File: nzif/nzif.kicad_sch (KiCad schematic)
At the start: 16 parts, among them J1 Rx, J10 ADAU1467_GPIOS, J11 ADAU1467_AUX_ADCS, J201 Rx, J4 6V, J6 Microcontroller, J7 USBi, J8 I2S2, J9 I2S1

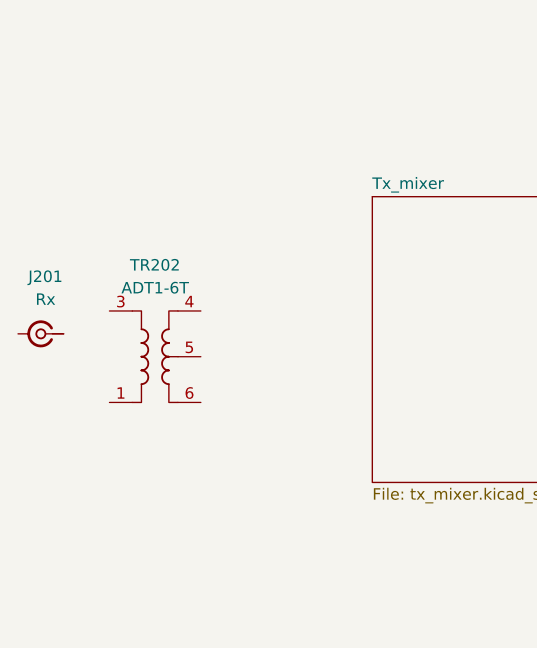
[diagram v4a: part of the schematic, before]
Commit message: added transformer for low band tx
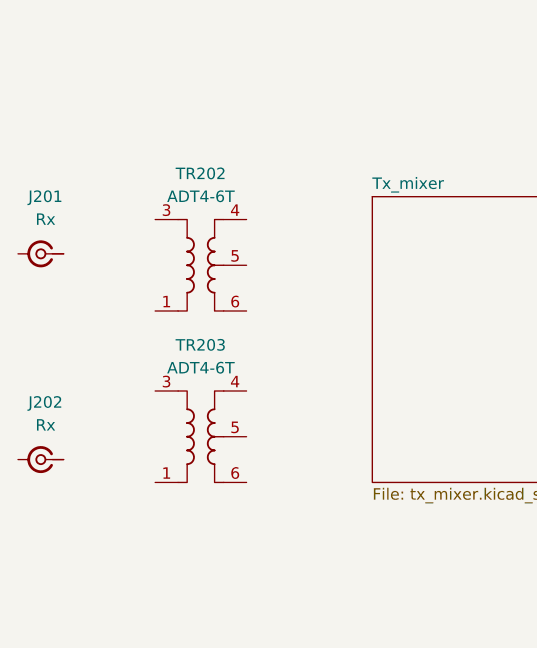
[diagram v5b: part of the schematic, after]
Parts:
- removed TR202: ADT1-6T, RF_Mini-Circuits:Mini-Circuits_CD637_H5.23mm, symbol Transformer:ADT1-6T
- added J202: Rx, symbol Connector:Conn_Coaxial_Small
- added TR202, TR203: ADT4-6T, RF_Mini-Circuits:Mini-Circuits_CD637_H5.23mm, symbol Transformer:ADT4-6T
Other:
- moved on the sheet: J201
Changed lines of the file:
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@@
+	)
+	(symbol
+		(lib_id "Transformer:ADT4-6T")
+		(at 46.99 144.78 0)
+		(unit 1)
+		(exclude_from_sim no)
+		(in_bom yes)
+		(on_board yes)
+		(dnp no)
+		(fields_autoplaced yes)
+		(property "Reference" "TR202"
+			(at 46.99 134.62 0)
+			(effects
+				(font
+					(size 1.27 1.27)
+				)
+			)
+		)
+		(property "Value" "ADT4-6T"
+			(at 46.99 137.16 0)
+			(effects
+				(font
+					(size 1.27 1.27)
+				)
+			)
+		)
+		(property "Footprint" "RF_Mini-Circuits:Mini-Circuits_CD637_H5.23mm"
+			(at 46.99 153.67 0)
+			(effects
+				(font
+					(size 1.27 1.27)
+				)
+				(hide yes)
+			)
+		)
+		(property "Datasheet" "https://www.minicircuits.com/pdfs/ADT4-6T+.pdf"
+			(at 46.99 144.78 0)
+			(effects
+				(font
+					(size 1.27 1.27)
+				)
+				(hide yes)
+			)
+		)
+		(property "Description" "1.5-70MHz 1:4 RF Transformer, Unbalanced to Balanced Center Tap, CD637"
+			(at 46.99 144.78 0)
+			(effects
+				(font
+					(size 1.27 1.27)
+				)
+				(hide yes)
+			)
+		)
+		(pin "3"
+		)
+		(pin "4"
+		)
+		(pin "6"
+		)
+		(pin "1"
+		)
+		(pin "5"
+		)
+		(instances
+			(project "nzif"
+				(path "/fe42ca2f-2bb8-4d5a-9e84-807788ed632f"
+					(reference "TR202")
+					(unit 1)
+				)
+			)
+		)
 	)
 	(symbol
@@
 	)
 	(symbol
-		(lib_id "Transformer:ADT1-6T")
-		(at 41.91 154.94 0)
-		(unit 1)
-		(exclude_from_sim no)
-		(in_bom yes)
-		(on_board yes)
-		(dnp no)
-		(fields_autoplaced yes)
-		(property "Reference" "TR202"
-			(at 41.91 144.78 0)
-			(effects
-				(font
-					(size 1.27 1.27)
-				)
-			)
-		)
-		(property "Value" "ADT1-6T"
-			(at 41.91 147.32 0)
-			(effects
-				(font
-					(size 1.27 1.27)
-				)
-			)
-		)
-		(property "Footprint" "RF_Mini-Circuits:Mini-Circuits_CD637_H5.23mm"
-			(at 41.91 163.83 0)
-			(effects
-				(font
-					(size 1.27 1.27)
-				)
-				(hide yes)
-			)
-		)
-		(property "Datasheet" "https://www.minicircuits.com/pdfs/ADT1-6T+.pdf"
-			(at 41.91 154.94 0)
-			(effects
-				(font
-					(size 1.27 1.27)
-				)
-				(hide yes)
-			)
-		)
-		(property "Description" "0.06-160MHz 1:1 RF Transformer, Unbalanced to Balanced Center Tap, CD542"
-			(at 41.91 154.94 0)
-			(effects
-				(font
-					(size 1.27 1.27)
-				)
-				(hide yes)
-			)
-		)
-		(pin "1"
-		)
-		(pin "5"
-		)
-		(pin "4"
-		)
-		(pin "6"
-		)
-		(pin "3"
-		)
-		(instances
-			(project "nzif"
-				(path "/fe42ca2f-2bb8-4d5a-9e84-807788ed632f"
-					(reference "TR202")
-					(unit 1)
-				)
-			)
-		)
-	)
-	(symbol
 		(lib_id "Device:R_Small_US")
 		(at 398.78 45.72 270)
@@
 	)
 	(symbol
+		(lib_id "Connector:Conn_Coaxial_Small")
+		(at 29.21 166.37 180)
+		(unit 1)
+		(exclude_from_sim no)
+		(in_bom yes)
+		(on_board yes)
+		(dnp no)
+		(fields_autoplaced yes)
+		(property "Reference" "J202"
+			(at 29.7295 160.02 0)
+			(effects
+				(font
+					(size 1.27 1.27)
+				)
+			)
+		)
+		(property "Value" "Rx"
+			(at 29.7295 162.56 0)
+			(effects
+				(font
+					(size 1.27 1.27)
+				)
+			)
+		)
+		(property "Footprint" ""
+			(at 29.21 166.37 0)
+			(effects
+				(font
+					(size 1.27 1.27)
+				)
+				(hide yes)
+			)
+		)
+		(property "Datasheet" "~"
+			(at 29.21 166.37 0)
+			(effects
+				(font
+					(size 1.27 1.27)
+				)
+				(hide yes)
+			)
+		)
+		(property "Description" "small coaxial connector (BNC, SMA, SMB, SMC, Cinch/RCA, LEMO, ...)"
+			(at 29.21 166.37 0)
+			(effects
+				(font
+					(size 1.27 1.27)
+				)
+				(hide yes)
+			)
+		)
+		(pin "2"
+		)
+		(pin "1"
+		)
+		(instances
+			(project "nzif"
+				(path "/fe42ca2f-2bb8-4d5a-9e84-807788ed632f"
+					(reference "J202")
+					(unit 1)
+				)
+			)
+		)
+	)
+	(symbol
 		(lib_id "Device:LED_Small_Filled")
 		(at 440.69 58.42 90)
@@
 	(symbol
 		(lib_id "Connector:Conn_Coaxial_Small")
-		(at 29.21 152.4 180)
+		(at 29.21 143.51 180)
 		(unit 1)
 		(exclude_from_sim no)
@@
 		(fields_autoplaced yes)
 		(property "Reference" "J201"
-			(at 29.7295 146.05 0)
+			(at 29.7295 137.16 0)
 			(effects
 				(font
@@
 		)
 		(property "Value" "Rx"
-			(at 29.7295 148.59 0)
-			(effects
-				(font
-					(size 1.27 1.27)
-				)
-			)
-		)
-		(property "Footprint" ""
-			(at 29.21 152.4 0)
+			(at 29.7295 139.7 0)
+			(effects
+				(font
+					(size 1.27 1.27)
+				)
+			)
+		)
+		(property "Footprint" ""
+			(at 29.21 143.51 0)
 			(effects
 				(font
@@
 		)
 		(property "Datasheet" "~"
-			(at 29.21 152.4 0)
+			(at 29.21 143.51 0)
 			(effects
 				(font
@@
 		)
 		(property "Description" "small coaxial connector (BNC, SMA, SMB, SMC, Cinch/RCA, LEMO, ...)"
-			(at 29.21 152.4 0)
+			(at 29.21 143.51 0)
 			(effects
 				(font
@@
 					(unit 1)
 				)
+			)
+		)
+	)
+	(symbol
+		(lib_id "Transformer:ADT4-6T")
+		(at 46.99 163.83 0)
+		(unit 1)
+		(exclude_from_sim no)
+		(in_bom yes)
+		(on_board yes)
+		(dnp no)
+		(fields_autoplaced yes)
+		(property "Reference" "TR203"
+			(at 46.99 153.67 0)
+			(effects
+				(font
+					(size 1.27 1.27)
+				)
+			)
+		)
+		(property "Value" "ADT4-6T"
+			(at 46.99 156.21 0)
+			(effects
+				(font
+					(size 1.27 1.27)
+				)
+			)
+		)
+		(property "Footprint" "RF_Mini-Circuits:Mini-Circuits_CD637_H5.23mm"
+			(at 46.99 172.72 0)
+			(effects
+				(font
+					(size 1.27 1.27)
+				)
+				(hide yes)
+			)
+		)
+		(property "Datasheet" "https://www.minicircuits.com/pdfs/ADT4-6T+.pdf"
+			(at 46.99 163.83 0)
+			(effects
+				(font
+					(size 1.27 1.27)
+				)
+				(hide yes)
+			)
+		)
+		(property "Description" "1.5-70MHz 1:4 RF Transformer, Unbalanced to Balanced Center Tap, CD637"
+			(at 46.99 163.83 0)
+			(effects
+				(font
+					(size 1.27 1.27)
+				)
+				(hide yes)
+			)
+		)
+		(pin "3"
+		)
+		(pin "4"
+		)
+		(pin "6"
+		)
+		(pin "1"
+		)
+		(pin "5"
+		)
+		(instances
+			(project "nzif"
+				(path "/fe42ca2f-2bb8-4d5a-9e84-807788ed632f"
+					(reference "TR203")
+					(unit 1)
+				)

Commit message: adjusted top level block positions
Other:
- moved on the sheet: D?, J10, J11, J8, J9, J?, R218, R219

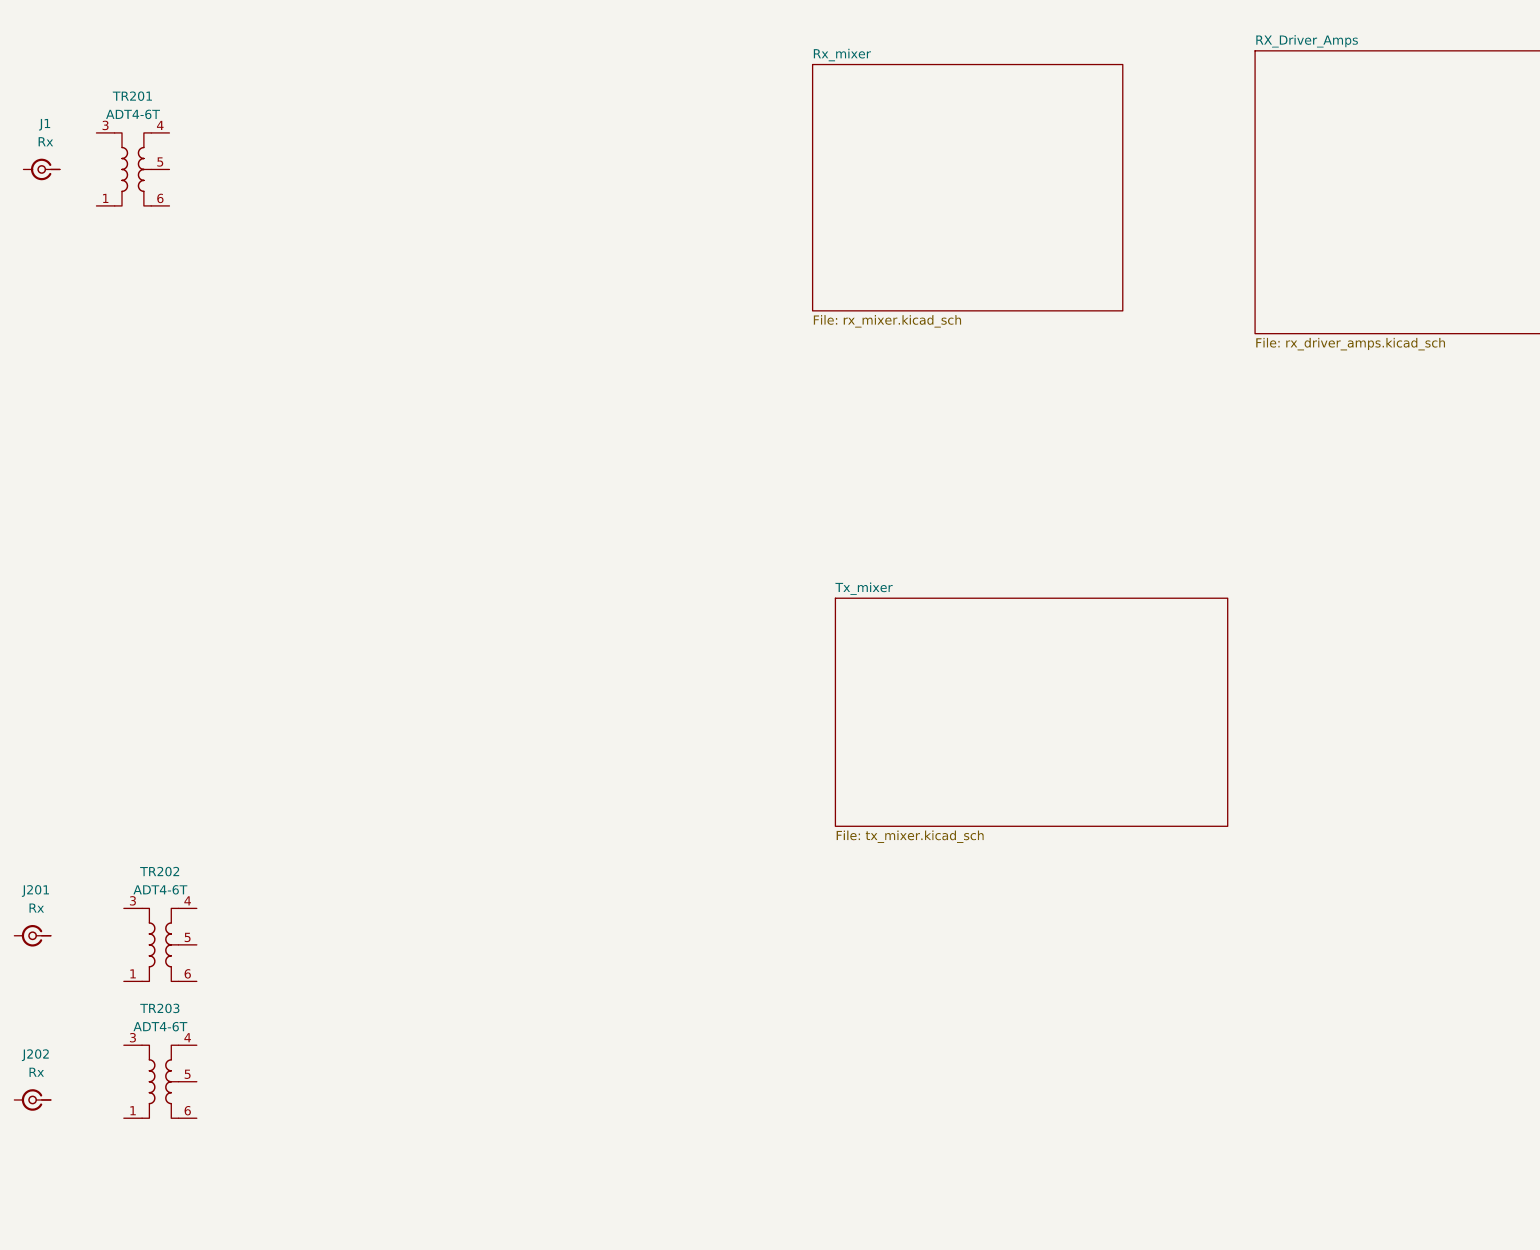
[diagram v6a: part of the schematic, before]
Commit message: added ad9912
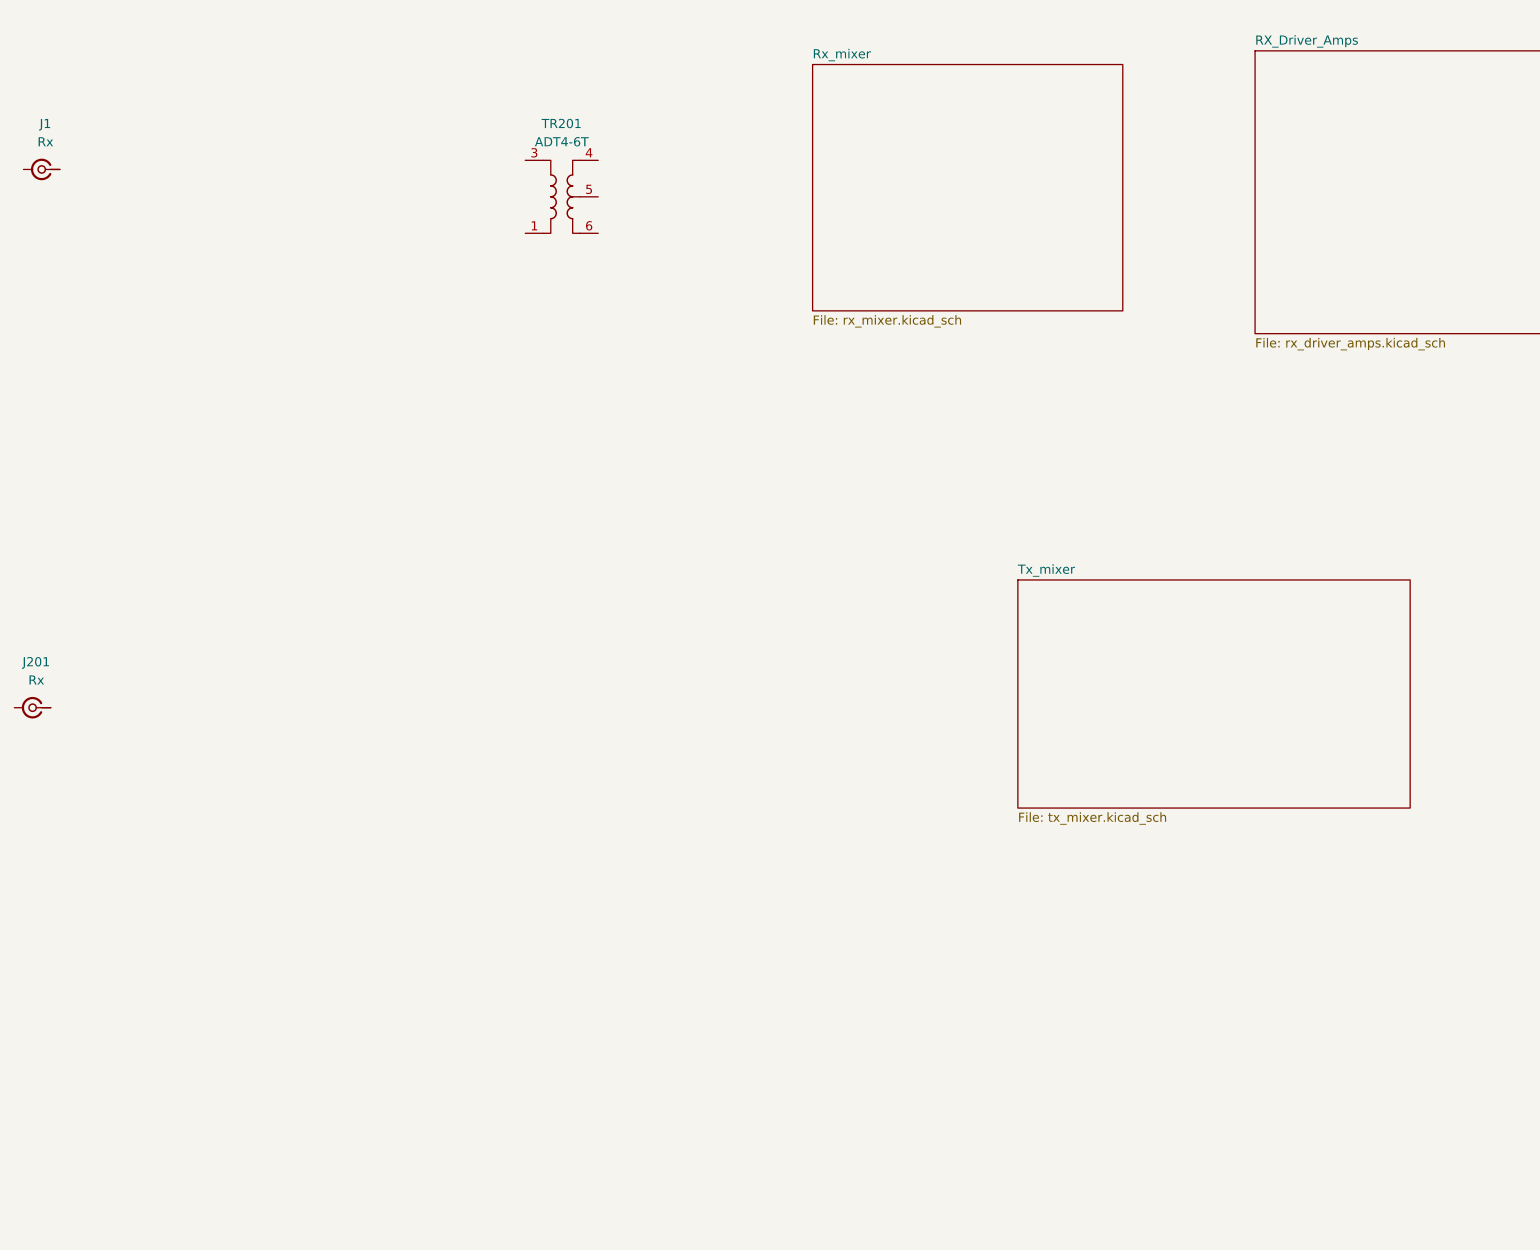
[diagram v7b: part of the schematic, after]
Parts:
- removed J202: Rx, symbol Connector:Conn_Coaxial_Small
- removed TR202, TR203: ADT4-6T, RF_Mini-Circuits:Mini-Circuits_CD637_H5.23mm, symbol Transformer:ADT4-6T
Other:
- moved on the sheet: J201, TR201
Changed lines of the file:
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@@
-	)
-	(symbol
-		(lib_id "Transformer:ADT4-6T")
-		(at 46.99 144.78 0)
-		(unit 1)
-		(exclude_from_sim no)
-		(in_bom yes)
-		(on_board yes)
-		(dnp no)
-		(fields_autoplaced yes)
-		(property "Reference" "TR202"
-			(at 46.99 134.62 0)
-			(effects
-				(font
-					(size 1.27 1.27)
-				)
-			)
-		)
-		(property "Value" "ADT4-6T"
-			(at 46.99 137.16 0)
-			(effects
-				(font
-					(size 1.27 1.27)
-				)
-			)
-		)
-		(property "Footprint" "RF_Mini-Circuits:Mini-Circuits_CD637_H5.23mm"
-			(at 46.99 153.67 0)
-			(effects
-				(font
-					(size 1.27 1.27)
-				)
-				(hide yes)
-			)
-		)
-		(property "Datasheet" "https://www.minicircuits.com/pdfs/ADT4-6T+.pdf"
-			(at 46.99 144.78 0)
-			(effects
-				(font
-					(size 1.27 1.27)
-				)
-				(hide yes)
-			)
-		)
-		(property "Description" "1.5-70MHz 1:4 RF Transformer, Unbalanced to Balanced Center Tap, CD637"
-			(at 46.99 144.78 0)
-			(effects
-				(font
-					(size 1.27 1.27)
-				)
-				(hide yes)
-			)
-		)
-		(pin "3"
-		)
-		(pin "4"
-		)
-		(pin "6"
-		)
-		(pin "1"
-		)
-		(pin "5"
-		)
-		(instances
-			(project "nzif"
-				(path "/fe42ca2f-2bb8-4d5a-9e84-807788ed632f"
-					(reference "TR202")
-					(unit 1)
-				)
-			)
-		)
 	)
 	(symbol
@@
 	)
 	(symbol
-		(lib_id "Connector:Conn_Coaxial_Small")
-		(at 29.21 166.37 180)
-		(unit 1)
-		(exclude_from_sim no)
-		(in_bom yes)
-		(on_board yes)
-		(dnp no)
-		(fields_autoplaced yes)
-		(property "Reference" "J202"
-			(at 29.7295 160.02 0)
-			(effects
-				(font
-					(size 1.27 1.27)
-				)
-			)
-		)
-		(property "Value" "Rx"
-			(at 29.7295 162.56 0)
-			(effects
-				(font
-					(size 1.27 1.27)
-				)
-			)
-		)
-		(property "Footprint" ""
-			(at 29.21 166.37 0)
-			(effects
-				(font
-					(size 1.27 1.27)
-				)
-				(hide yes)
-			)
-		)
-		(property "Datasheet" "~"
-			(at 29.21 166.37 0)
-			(effects
-				(font
-					(size 1.27 1.27)
-				)
-				(hide yes)
-			)
-		)
-		(property "Description" "small coaxial connector (BNC, SMA, SMB, SMC, Cinch/RCA, LEMO, ...)"
-			(at 29.21 166.37 0)
-			(effects
-				(font
-					(size 1.27 1.27)
-				)
-				(hide yes)
-			)
-		)
-		(pin "2"
-		)
-		(pin "1"
-		)
-		(instances
-			(project "nzif"
-				(path "/fe42ca2f-2bb8-4d5a-9e84-807788ed632f"
-					(reference "J202")
-					(unit 1)
-				)
-			)
-		)
-	)
-	(symbol
 		(lib_id "Device:LED_Small_Filled")
 		(at 403.86 49.53 90)
@@
 	(symbol
 		(lib_id "Connector:Conn_Coaxial_Small")
-		(at 29.21 143.51 180)
+		(at 29.21 111.76 180)
 		(unit 1)
 		(exclude_from_sim no)
@@
 		(fields_autoplaced yes)
 		(property "Reference" "J201"
-			(at 29.7295 137.16 0)
+			(at 29.7295 105.41 0)
 			(effects
 				(font
@@
 		)
 		(property "Value" "Rx"
-			(at 29.7295 139.7 0)
-			(effects
-				(font
-					(size 1.27 1.27)
-				)
-			)
-		)
-		(property "Footprint" ""
-			(at 29.21 143.51 0)
+			(at 29.7295 107.95 0)
+			(effects
+				(font
+					(size 1.27 1.27)
+				)
+			)
+		)
+		(property "Footprint" ""
+			(at 29.21 111.76 0)
 			(effects
 				(font
@@
 		)
 		(property "Datasheet" "~"
-			(at 29.21 143.51 0)
+			(at 29.21 111.76 0)
 			(effects
 				(font
@@
 		)
 		(property "Description" "small coaxial connector (BNC, SMA, SMB, SMC, Cinch/RCA, LEMO, ...)"
-			(at 29.21 143.51 0)
+			(at 29.21 111.76 0)
 			(effects
 				(font
@@
 	)
 	(symbol
-		(lib_id "Transformer:ADT4-6T")
-		(at 46.99 163.83 0)
-		(unit 1)
-		(exclude_from_sim no)
-		(in_bom yes)
-		(on_board yes)
-		(dnp no)
-		(fields_autoplaced yes)
-		(property "Reference" "TR203"
-			(at 46.99 153.67 0)
-			(effects
-				(font
-					(size 1.27 1.27)
-				)
-			)
-		)
-		(property "Value" "ADT4-6T"
-			(at 46.99 156.21 0)
-			(effects
-				(font
-					(size 1.27 1.27)
-				)
-			)
-		)
-		(property "Footprint" "RF_Mini-Circuits:Mini-Circuits_CD637_H5.23mm"
-			(at 46.99 172.72 0)
-			(effects
-				(font
-					(size 1.27 1.27)
-				)
-				(hide yes)
-			)
-		)
-		(property "Datasheet" "https://www.minicircuits.com/pdfs/ADT4-6T+.pdf"
-			(at 46.99 163.83 0)
-			(effects
-				(font
-					(size 1.27 1.27)
-				)
-				(hide yes)
-			)
-		)
-		(property "Description" "1.5-70MHz 1:4 RF Transformer, Unbalanced to Balanced Center Tap, CD637"
-			(at 46.99 163.83 0)
-			(effects
-				(font
-					(size 1.27 1.27)
-				)
-				(hide yes)
-			)
-		)
-		(pin "3"
-		)
-		(pin "4"
-		)
-		(pin "6"
-		)
-		(pin "1"
-		)
-		(pin "5"
-		)
-		(instances
-			(project "nzif"
-				(path "/fe42ca2f-2bb8-4d5a-9e84-807788ed632f"
-					(reference "TR203")
-					(unit 1)
-				)
-			)
-		)
-	)
-	(symbol
 		(lib_id "power:GND")
 		(at 382.27 45.72 0)
@@
 	(symbol
 		(lib_id "Transformer:ADT4-6T")
-		(at 43.18 36.83 0)
+		(at 102.87 40.64 0)
 		(unit 1)
 		(exclude_from_sim no)
@@
 		(fields_autoplaced yes)
 		(property "Reference" "TR201"
-			(at 43.18 26.67 0)
+			(at 102.87 30.48 0)
 			(effects
 				(font
@@
 		)
 		(property "Value" "ADT4-6T"
-			(at 43.18 29.21 0)
+			(at 102.87 33.02 0)
 			(effects
 				(font
@@
 		)
 		(property "Footprint" "RF_Mini-Circuits:Mini-Circuits_CD637_H5.23mm"
-			(at 43.18 45.72 0)
+			(at 102.87 49.53 0)
 			(effects
 				(font
@@
 		)
 		(property "Datasheet" "https://www.minicircuits.com/pdfs/ADT4-6T+.pdf"
-			(at 43.18 36.83 0)
+			(at 102.87 40.64 0)
 			(effects
 				(font
@@
 		)
 		(property "Description" "1.5-70MHz 1:4 RF Transformer, Unbalanced to Balanced Center Tap, CD637"
-			(at 43.18 36.83 0)
+			(at 102.87 40.64 0)
 			(effects
 				(font
@@
 	)
 	(sheet
-		(at 140.97 96.52)
+		(at 166.37 93.98)
 		(size 54.61 31.75)
 		(exclude_from_sim no)
@@
 		)
 		(property "Sheetname" "Tx_mixer"
-			(at 140.97 95.8084 0)
+			(at 166.37 93.2684 0)
 			(effects
 				(font
@@
 		)
 		(property "Sheetfile" "tx_mixer.kicad_sch"
-			(at 140.97 128.8546 0)
-			(effects
-				(font
+			(at 166.37 126.3146 0)
+			(effects
+				(font
